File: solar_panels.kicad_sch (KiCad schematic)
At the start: 72 parts, among them U21 MAX40200AUK, U22 BQ25570RGRR, U23 MAX40200AUK, U24 BQ25570RGRR

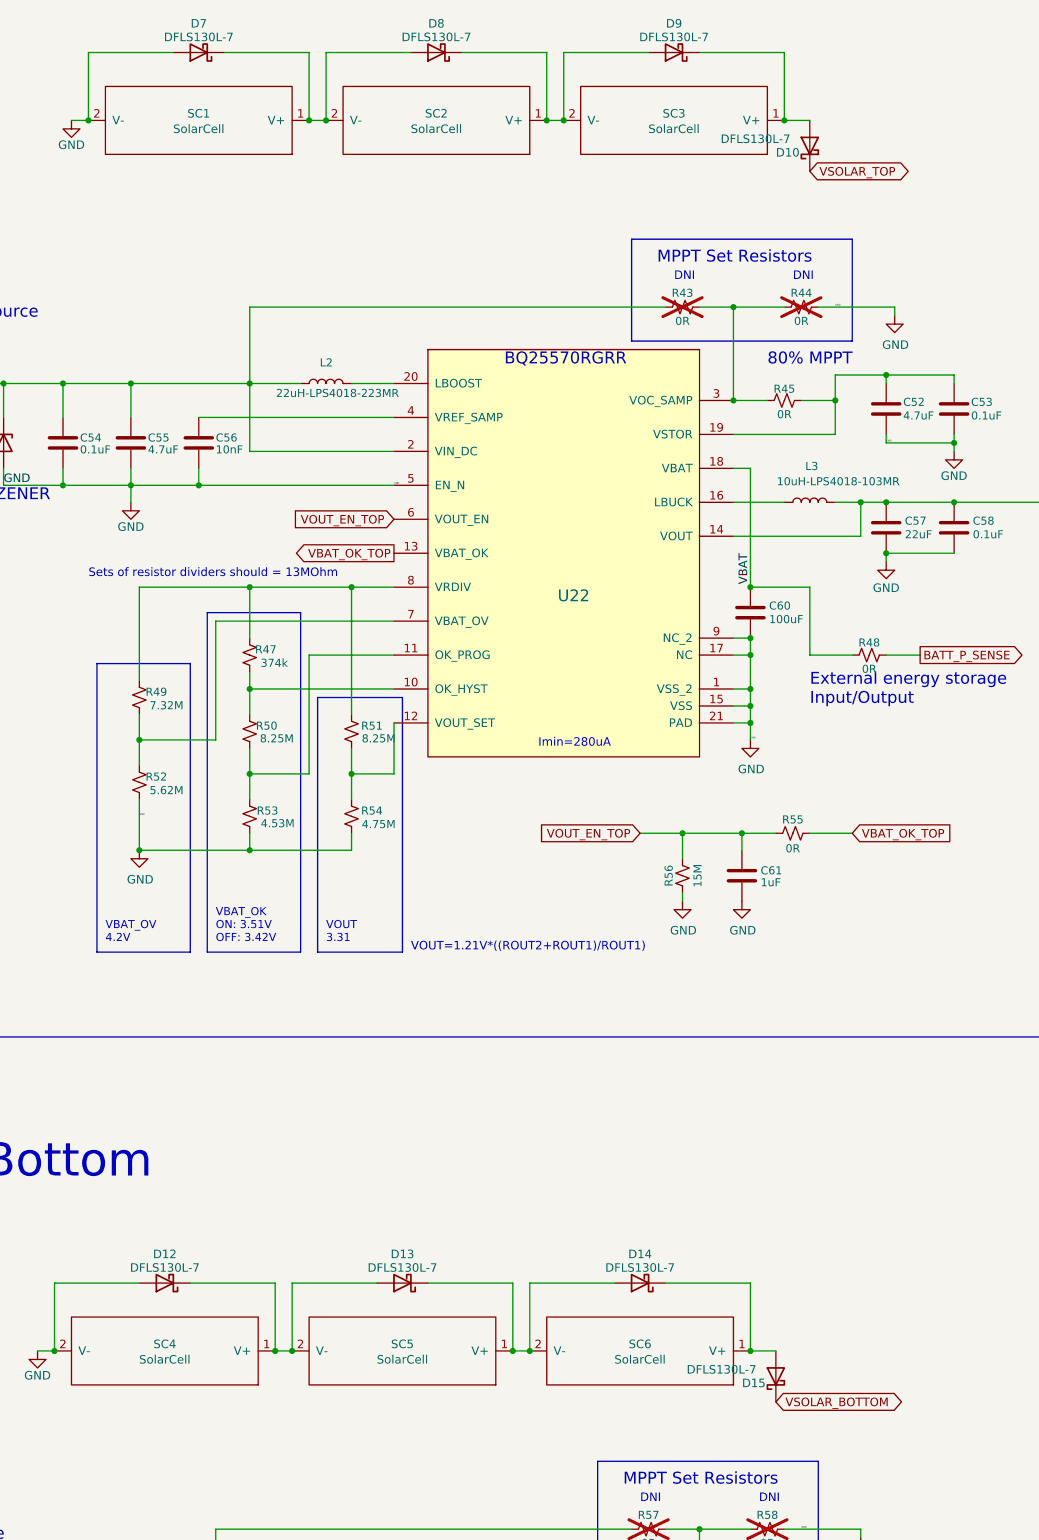
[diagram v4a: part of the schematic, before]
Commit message: Update solar panel analysis to keep all components in front
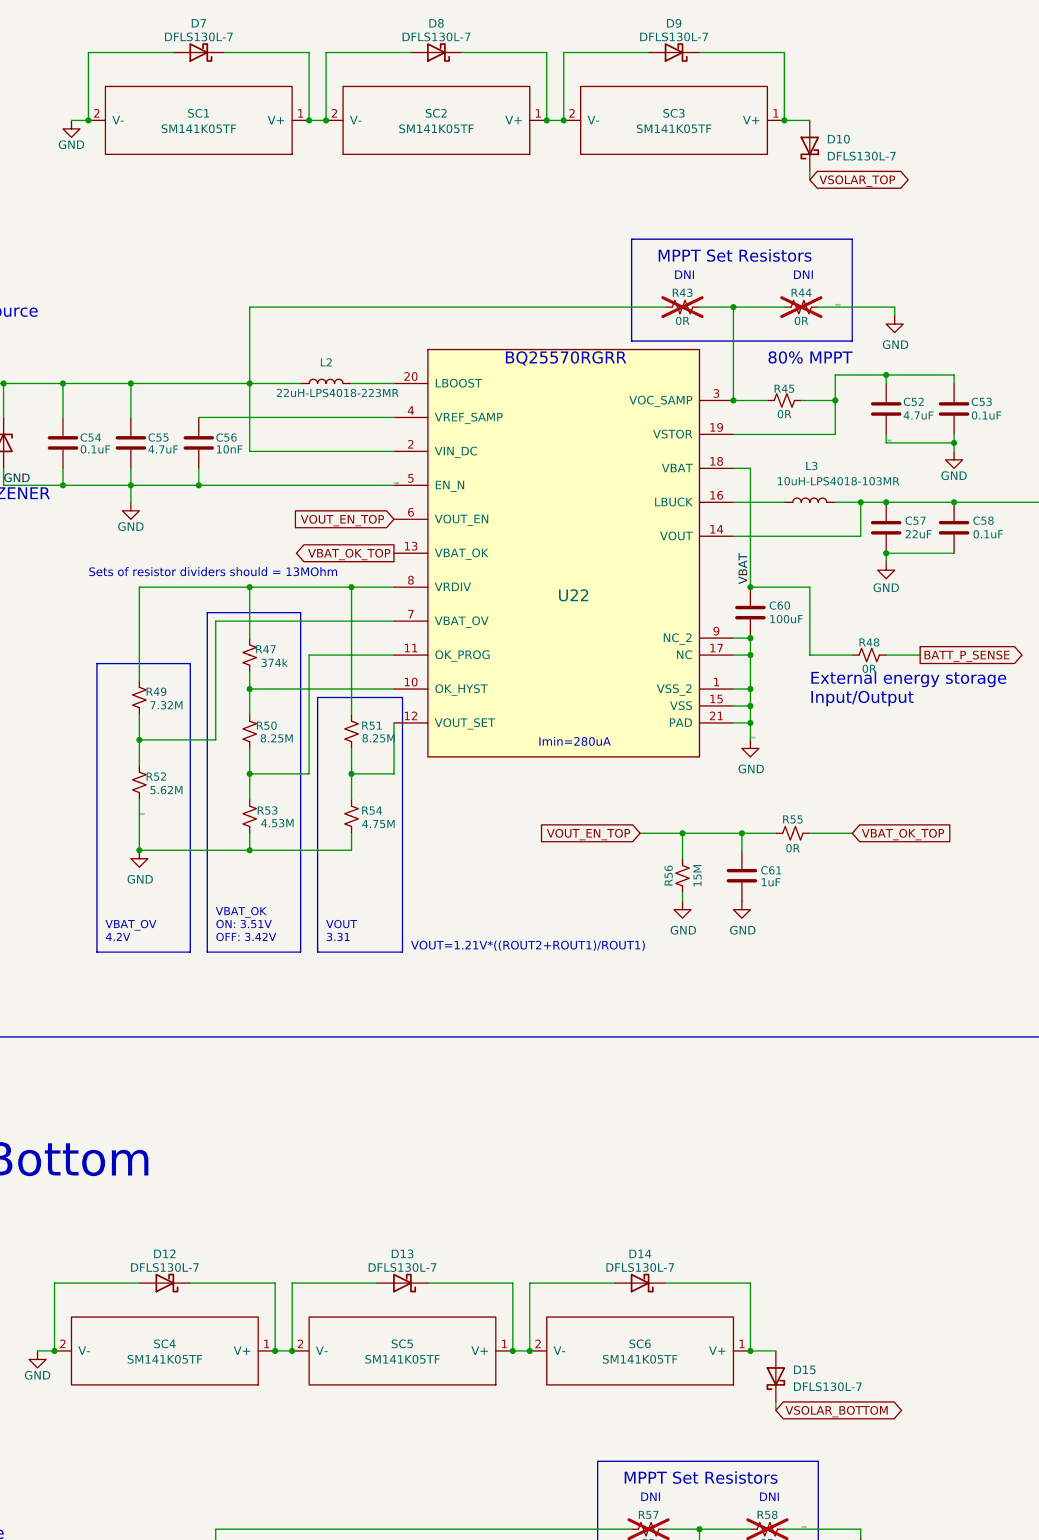
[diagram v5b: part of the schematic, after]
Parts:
- SC1, SC2, SC3, SC4, SC5, SC6: value SolarCell -> SM141K05TF; footprint solarpanels:KXOB25-05X3F -> solarpanels:SM141K05TF; Manufacturer_Part_Number (none) -> SM141K05TF
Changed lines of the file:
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@@
 	(wire
 		(pts
+			(xy 190.5 62.23) (xy 190.5 60.96)
+		)
+		(stroke
+			(width 0)
+			(type default)
+		)
+	)
+	(wire
+		(pts
 			(xy 73.66 275.59) (xy 73.66 280.67)
 		)
@@
 	(wire
 		(pts
+			(xy 185.42 246.38) (xy 185.42 245.11)
+		)
+		(stroke
+			(width 0)
+			(type default)
+		)
+	)
+	(wire
+		(pts
 			(xy 190.5 123.19) (xy 181.61 123.19)
 		)
@@
 	(global_label "VSOLAR_TOP"
 		(shape bidirectional)
-		(at 190.5 60.96 0)
+		(at 190.5 62.23 0)
 		(fields_autoplaced yes)
 		(effects
@@
 		)
 		(property "Intersheetrefs" "${INTERSHEET_REFS}"
-			(at 206.1475 60.96 0)
+			(at 206.1475 62.23 0)
 			(effects
 				(font
@@
 	(global_label "VSOLAR_BOTTOM"
 		(shape bidirectional)
-		(at 185.42 245.11 0)
+		(at 185.42 246.38 0)
 		(fields_autoplaced yes)
 		(effects
@@
 		)
 		(property "Intersheetrefs" "${INTERSHEET_REFS}"
-			(at 204.817 245.11 0)
+			(at 204.817 246.38 0)
 			(effects
 				(font
@@
 		(on_board yes)
 		(dnp no)
+		(fields_autoplaced yes)
 		(property "Reference" "D10"
-			(at 187.198 58.166 90)
+			(at 193.04 56.1974 90)
 			(effects
 				(font
 					(size 1.27 1.27)
 				)
+				(justify right)
 			)
 		)
 		(property "Value" "DFLS130L-7"
-			(at 182.372 56.134 90)
+			(at 193.04 58.7374 90)
 			(effects
 				(font
 					(size 1.27 1.27)
 				)
+				(justify right)
 			)
 		)
@@
 			)
 		)
-		(property "Value" "SolarCell"
+		(property "Value" "SM141K05TF"
 			(at 165.1 238.7854 0)
 			(effects
@@
 			)
 		)
-		(property "Footprint" "solarpanels:KXOB25-05X3F"
+		(property "Footprint" "solarpanels:SM141K05TF"
 			(at 165.1 231.14 0)
 			(effects
@@
 			)
 		)
-		(property "Datasheet" ""
+		(property "Datasheet" "https://waf-e.dubudisk.com/anysolar.dubuplus.com/techsupport@anysolar.biz/O18BDYP/DubuDisk/www/Gen3/SM141K05TF%20DATA%20SHEET%20202105.pdf"
 			(at 160.02 237.49 90)
 			(effects
@@
 			)
 		)
+		(property "Manufacturer_Part_Number" "SM141K05TF"
+			(at 165.1 237.49 0)
+			(effects
+				(font
+					(size 1.27 1.27)
+				)
+				(hide yes)
+			)
+		)
 		(pin "1"
 		)
@@
 		(on_board yes)
 		(dnp no)
+		(fields_autoplaced yes)
 		(property "Reference" "D15"
-			(at 182.118 242.316 90)
+			(at 187.96 240.3474 90)
 			(effects
 				(font
 					(size 1.27 1.27)
 				)
+				(justify right)
 			)
 		)
 		(property "Value" "DFLS130L-7"
-			(at 177.292 240.284 90)
+			(at 187.96 242.8874 90)
 			(effects
 				(font
 					(size 1.27 1.27)
 				)
+				(justify right)
 			)
 		)
@@
 			)
 		)
-		(property "Value" "SolarCell"
+		(property "Value" "SM141K05TF"
 			(at 134.62 54.6354 0)
 			(effects
@@
 			)
 		)
-		(property "Footprint" "solarpanels:KXOB25-05X3F"
+		(property "Footprint" "solarpanels:SM141K05TF"
 			(at 134.62 46.99 0)
 			(effects
@@
 			)
 		)
-		(property "Datasheet" ""
+		(property "Datasheet" "https://waf-e.dubudisk.com/anysolar.dubuplus.com/techsupport@anysolar.biz/O18BDYP/DubuDisk/www/Gen3/SM141K05TF%20DATA%20SHEET%20202105.pdf"
 			(at 129.54 53.34 90)
 			(effects
@@
 			)
 		)
+		(property "Manufacturer_Part_Number" "SM141K05TF"
+			(at 134.62 53.34 0)
+			(effects
+				(font
+					(size 1.27 1.27)
+				)
+				(hide yes)
+			)
+		)
 		(pin "1"
 		)
@@
 			)
 		)
-		(property "Value" "SolarCell"
+		(property "Value" "SM141K05TF"
 			(at 93.98 238.7854 0)
 			(effects
@@
 			)
 		)
-		(property "Footprint" "solarpanels:KXOB25-05X3F"
+		(property "Footprint" "solarpanels:SM141K05TF"
 			(at 93.98 231.14 0)
 			(effects
@@
 			)
 		)
-		(property "Datasheet" ""
+		(property "Datasheet" "https://waf-e.dubudisk.com/anysolar.dubuplus.com/techsupport@anysolar.biz/O18BDYP/DubuDisk/www/Gen3/SM141K05TF%20DATA%20SHEET%20202105.pdf"
 			(at 88.9 237.49 90)
 			(effects
@@
 			)
 		)
+		(property "Manufacturer_Part_Number" "SM141K05TF"
+			(at 93.98 237.49 0)
+			(effects
+				(font
+					(size 1.27 1.27)
+				)
+				(hide yes)
+			)
+		)
 		(pin "1"
 		)
@@
 			)
 		)
-		(property "Value" "SolarCell"
+		(property "Value" "SM141K05TF"
 			(at 129.54 238.7854 0)
 			(effects
@@
 			)
 		)
-		(property "Footprint" "solarpanels:KXOB25-05X3F"
+		(property "Footprint" "solarpanels:SM141K05TF"
 			(at 129.54 231.14 0)
 			(effects
@@
 			)
 		)
-		(property "Datasheet" ""
+		(property "Datasheet" "https://waf-e.dubudisk.com/anysolar.dubuplus.com/techsupport@anysolar.biz/O18BDYP/DubuDisk/www/Gen3/SM141K05TF%20DATA%20SHEET%20202105.pdf"
 			(at 124.46 237.49 90)
 			(effects
@@
 			)
 		)
+		(property "Manufacturer_Part_Number" "SM141K05TF"
+			(at 129.54 237.49 0)
+			(effects
+				(font
+					(size 1.27 1.27)
+				)
+				(hide yes)
+			)
+		)
 		(pin "1"
 		)
@@
 			)
 		)
-		(property "Value" "SolarCell"
+		(property "Value" "SM141K05TF"
 			(at 170.18 54.6354 0)
 			(effects
@@
 			)
 		)
-		(property "Footprint" "solarpanels:KXOB25-05X3F"
+		(property "Footprint" "solarpanels:SM141K05TF"
 			(at 170.18 46.99 0)
 			(effects
@@
 			)
 		)
-		(property "Datasheet" ""
+		(property "Datasheet" "https://waf-e.dubudisk.com/anysolar.dubuplus.com/techsupport@anysolar.biz/O18BDYP/DubuDisk/www/Gen3/SM141K05TF%20DATA%20SHEET%20202105.pdf"
 			(at 165.1 53.34 90)
 			(effects
@@
 			)
 		)
+		(property "Manufacturer_Part_Number" "SM141K05TF"
+			(at 170.18 53.34 0)
+			(effects
+				(font
+					(size 1.27 1.27)
+				)
+				(hide yes)
+			)
+		)
 		(pin "1"
 		)
@@
 			)
 		)
-		(property "Value" "SolarCell"
+		(property "Value" "SM141K05TF"
 			(at 99.06 54.6354 0)
 			(effects
@@
 			)
 		)
-		(property "Footprint" "solarpanels:KXOB25-05X3F"
+		(property "Footprint" "solarpanels:SM141K05TF"
 			(at 99.06 46.99 0)
 			(effects
@@
 			)
 		)
-		(property "Datasheet" ""
+		(property "Datasheet" "https://waf-e.dubudisk.com/anysolar.dubuplus.com/techsupport@anysolar.biz/O18BDYP/DubuDisk/www/Gen3/SM141K05TF%20DATA%20SHEET%20202105.pdf"
 			(at 93.98 53.34 90)
 			(effects
@@
 			(at 99.06 53.34 0)
 			(effects
+				(font
+					(size 1.27 1.27)
+				)
+				(hide yes)
+			)
+		)
+		(property "Manufacturer_Part_Number" "SM141K05TF"
+			(at 99.06 53.34 0)
+			(effects

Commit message: Use a single MPPT to save some space
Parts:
- removed C52, C55: 4.7uF, Capacitor_SMD:C_0603_1608Metric, symbol Device:C
- removed C53, C54, C58, C59: 0.1uF, Capacitor_SMD:C_0603_1608Metric, symbol Device:C
- removed C56: 10nF, Capacitor_SMD:C_0603_1608Metric, symbol Device:C
- removed C57: 22uF, Capacitor_SMD:C_0603_1608Metric, symbol Device:C
- removed C60: 100uF, Capacitor_SMD:C_0805_2012Metric, symbol Device:C
- removed C61: 1uF, Capacitor_SMD:C_0603_1608Metric, symbol Device:C
- removed D11: SZMM5Z5V1T1G, Diode_SMD:D_SOD-523, symbol Diode:Z1SMAxxx
- removed D14, D9: DFLS130L-7, Diode_SMD:D_PowerDI-123, symbol Device:D_Schottky
- removed L2: 22uH-LPS4018-223MR, solarpanels:LPS4018, symbol Device:L
- removed L3: 10uH-LPS4018-103MR, solarpanels:LPS4018, symbol Device:L
- removed R43, R44, R45, R46, R48, R55: 0R, Resistor_SMD:R_0603_1608Metric, symbol Device:R_Small_US
- removed R47: 374k, Resistor_SMD:R_0603_1608Metric, symbol Device:R_Small_US
- removed R49: 7.32M, Resistor_SMD:R_0603_1608Metric, symbol Device:R_Small_US
- removed R50, R51: 8.25M, Resistor_SMD:R_0603_1608Metric, symbol Device:R_Small_US
- removed R52: 5.62M, Resistor_SMD:R_0603_1608Metric, symbol Device:R_Small_US
- removed R53: 4.53M, Resistor_SMD:R_0603_1608Metric, symbol Device:R_Small_US
- removed R54: 4.75M, Resistor_SMD:R_0603_1608Metric, symbol Device:R_Small_US
- removed R56: 15M, Resistor_SMD:R_0603_1608Metric, symbol Device:R_Small_US
- removed SC3, SC6: SM141K05TF, solarpanels:SM141K05TF, symbol solarpanels:SolarCell_Small
- removed U21: MAX40200AUK, Package_TO_SOT_SMD:SOT-23-5, symbol Analog_Switch:MAX40200AUK
- removed U22: BQ25570RGRR, solarpanels:QFN50P350X350X100-21N-D, symbol solarpanels:BQ25570RGRR
- R69: now fitted
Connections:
- net at D10.2 (A): now also D8.1 (K), SC2.1 (V+)
- net at D15.2 (A): now also D13.1 (K), SC5.1 (V+)
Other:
- note added: "MPPT"
- moved on the sheet: C62, C63, C64, C65, C66, C67, C68, C69, C70, C71, D10, D12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

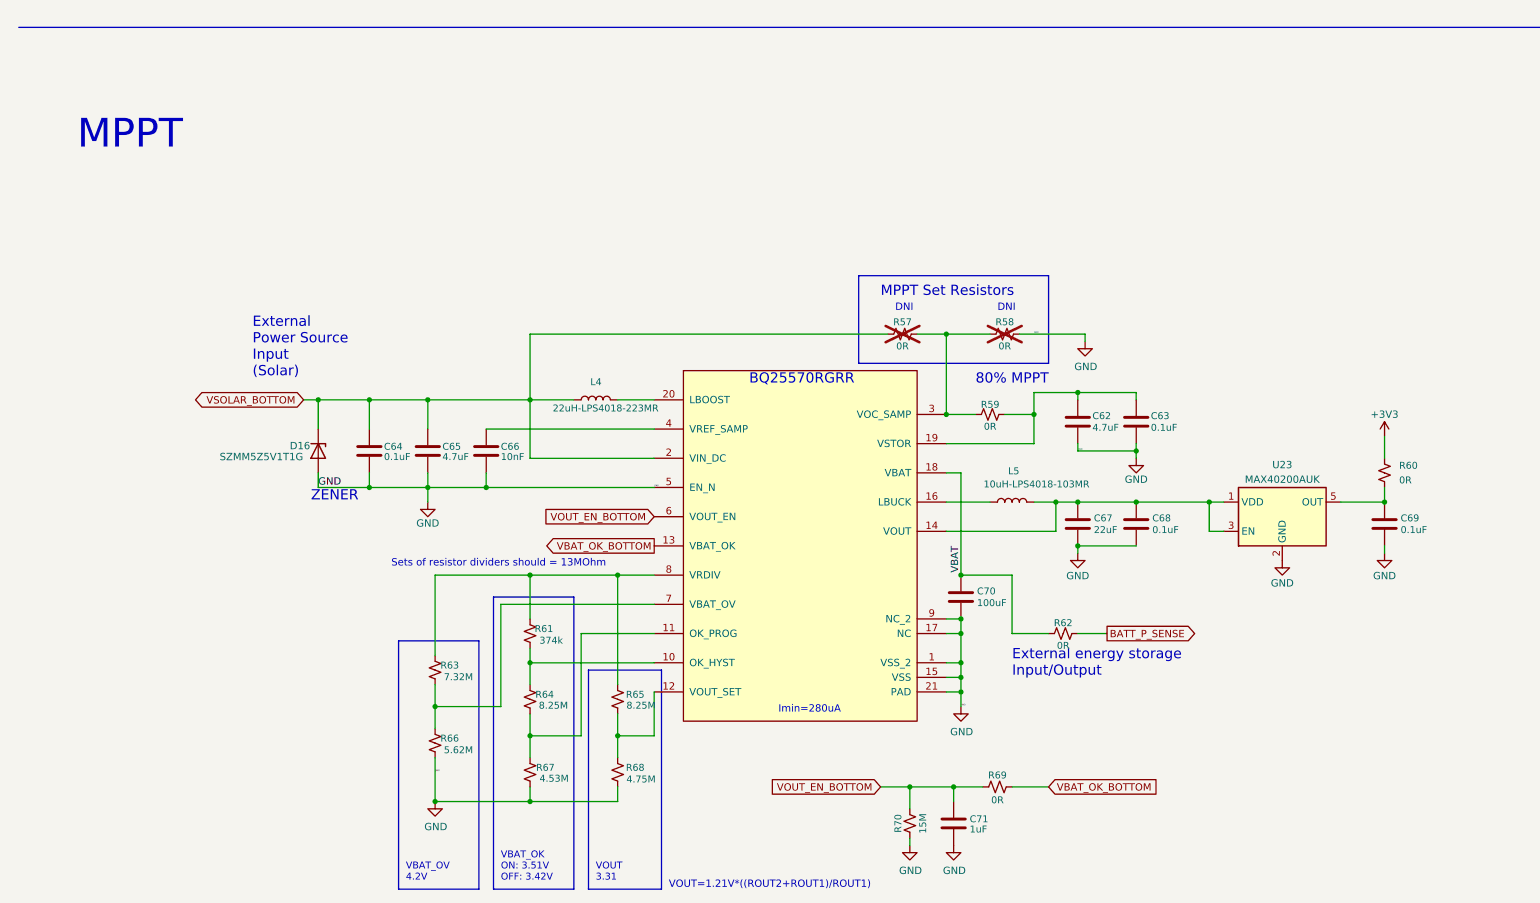
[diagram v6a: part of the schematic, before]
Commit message: Add battery connectors
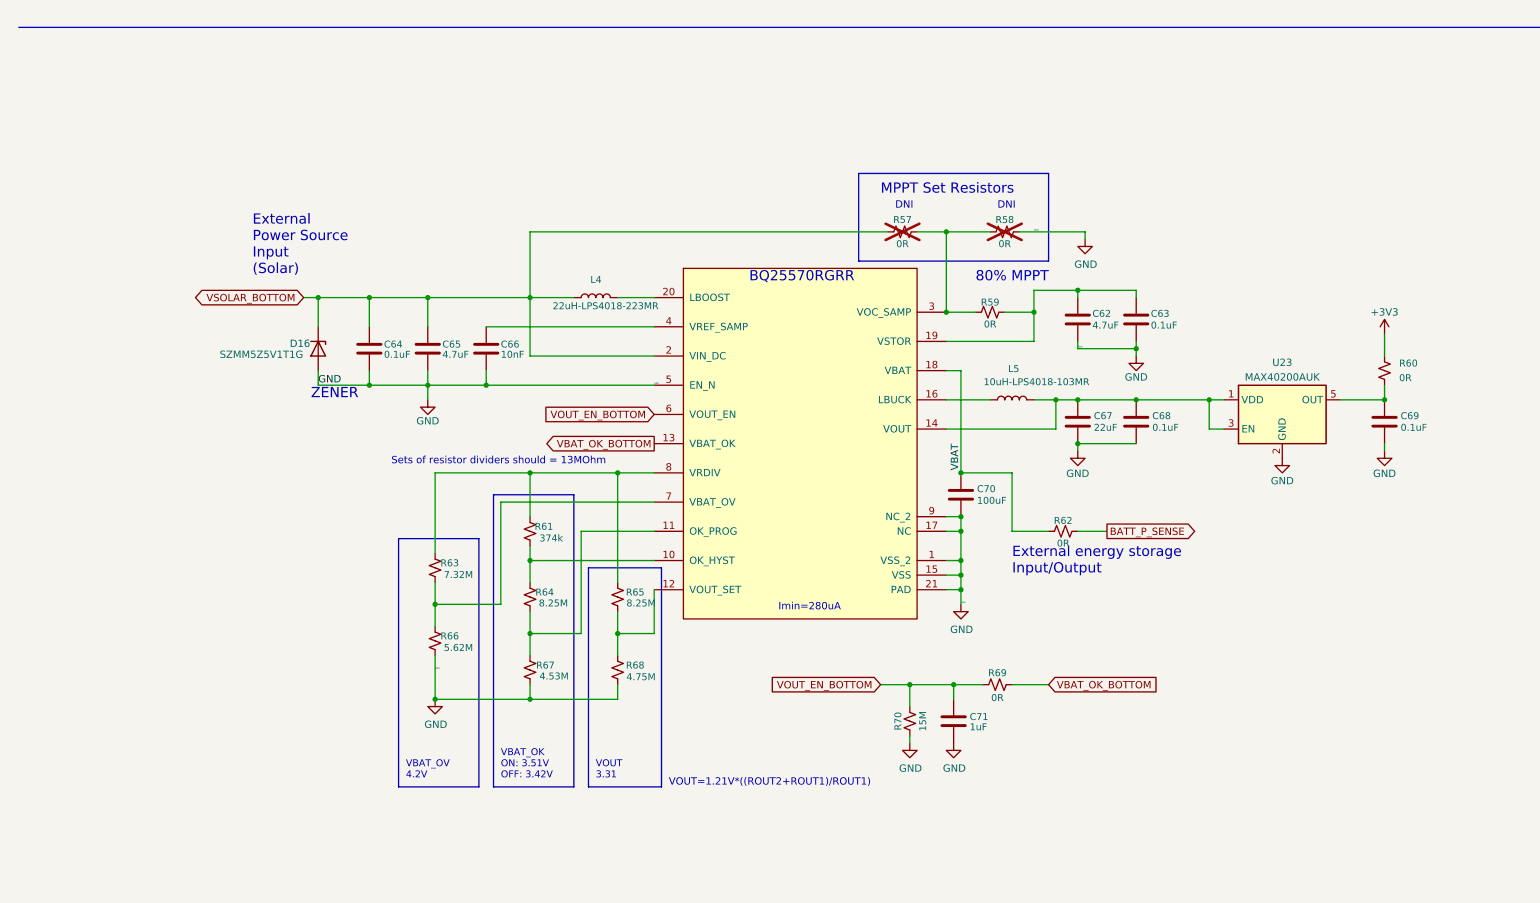
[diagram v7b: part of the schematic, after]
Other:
- note removed: "MPPT"
- moved on the sheet: C62, C63, C64, C65, C66, C67, C68, C69, C70, C71, D16, L4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
